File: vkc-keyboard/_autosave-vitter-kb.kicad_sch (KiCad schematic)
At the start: 70 parts, among them SW1 SW_SPST, SW10 SW_SPST, SW11 SW_SPST, SW12 SW_SPST, SW13 SW_SPST, SW14 SW_SPST, SW15 SW_SPST, SW16 SW_SPST, SW17 SW_SPST, SW18 SW_SPST, SW19 SW_SPST, SW2 SW_SPST, SW20 SW_SPST, SW21 SW_SPST, SW22 SW_SPST, SW23 SW_SPST, SW24 SW_SPST, SW25 SW_SPST, SW26 SW_SPST, SW27 SW_SPST, SW28 SW_SPST, SW29 SW_SPST, SW3 SW_SPST, SW30 SW_SPST, SW31 SW_SPST, SW32 SW_SPST, SW33 SW_SPST, SW34 SW_SPST, SW35 SW_SPST, SW4 SW_SPST, SW5 SW_SPST, SW6 SW_SPST, SW7 SW_SPST, SW8 SW_SPST, SW9 SW_SPST

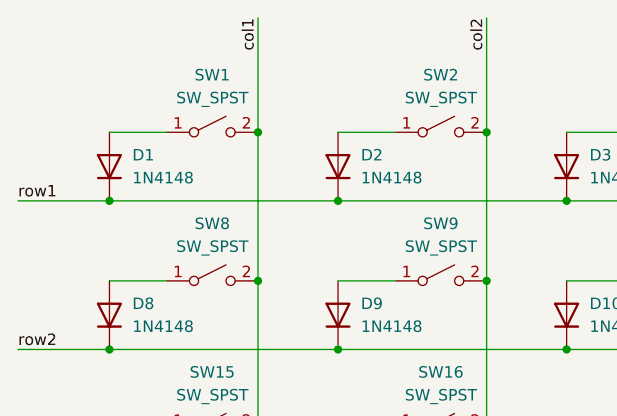
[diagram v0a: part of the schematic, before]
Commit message: use button outline footprint
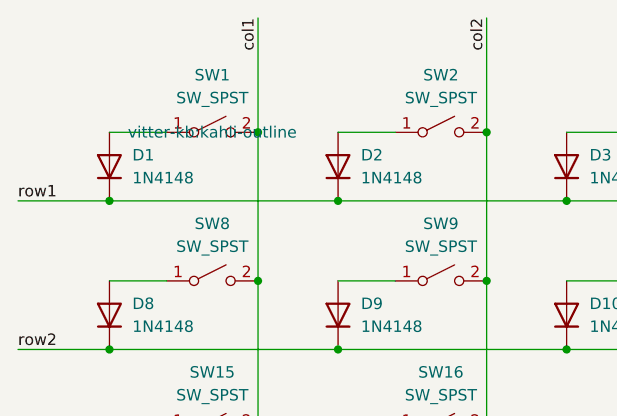
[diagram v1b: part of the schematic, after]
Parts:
- SW1, SW10, SW11, SW12, SW13, SW14, SW15, SW16, SW17, SW18, SW19, SW2, SW20, SW21, SW22, SW23, SW24, SW25, SW26, SW27, SW28, SW29, SW3, SW30, SW31, SW32, SW33, SW34, SW35, SW4, SW5, SW6, SW7, SW8, SW9: footprint vitter-kb:Kailh_socket_PG1350_reversible -> vitter-kb:kahli-outline
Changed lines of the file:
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@@
 			)
 		)
-		(property "Footprint" "vitter-kb:Kailh_socket_PG1350_reversible"
+		(property "Footprint" "vitter-kb:kahli-outline"
 			(at 196.85 38.1 0)
 			(effects
@@
 			)
 		)
-		(property "Footprint" "vitter-kb:Kailh_socket_PG1350_reversible"
+		(property "Footprint" "vitter-kb:kahli-outline"
 			(at 171.45 104.14 0)
 			(effects
@@
 			)
 		)
-		(property "Footprint" "vitter-kb:Kailh_socket_PG1350_reversible"
+		(property "Footprint" "vitter-kb:kahli-outline"
 			(at 95.25 54.61 0)
 			(effects
@@
 			)
 		)
-		(property "Footprint" "vitter-kb:Kailh_socket_PG1350_reversible"
+		(property "Footprint" "vitter-kb:kahli-outline"
 			(at 69.85 38.1 0)
 			(effects
@@
 			)
 		)
-		(property "Footprint" "vitter-kb:Kailh_socket_PG1350_reversible"
+		(property "Footprint" "vitter-kb:kahli-outline"
 			(at 95.25 71.12 0)
 			(effects
@@
 			)
 		)
-		(property "Footprint" "vitter-kb:Kailh_socket_PG1350_reversible"
+		(property "Footprint" "vitter-kb:kahli-outline"
 			(at 44.45 54.61 0)
 			(effects
@@
 			)
 		)
-		(property "Footprint" "vitter-kb:Kailh_socket_PG1350_reversible"
+		(property "Footprint" "vitter-kb:kahli-outline"
 			(at 69.85 87.63 0)
 			(effects
@@
 			)
 		)
-		(property "Footprint" "vitter-kb:Kailh_socket_PG1350_reversible"
+		(property "Footprint" "vitter-kb:kahli-outline"
 			(at 196.85 87.63 0)
 			(effects
@@
 			)
 		)
-		(property "Footprint" "vitter-kb:Kailh_socket_PG1350_reversible"
+		(property "Footprint" "vitter-kb:kahli-outline"
 			(at 171.45 38.1 0)
 			(effects
@@
 			)
 		)
-		(property "Footprint" "vitter-kb:Kailh_socket_PG1350_reversible"
+		(property "Footprint" "vitter-kb:kahli-outline"
 			(at 120.65 71.12 0)
 			(effects
@@
 			)
 		)
-		(property "Footprint" "vitter-kb:Kailh_socket_PG1350_reversible"
+		(property "Footprint" "vitter-kb:kahli-outline"
 			(at 120.65 104.14 0)
 			(effects
@@
 			)
 		)
-		(property "Footprint" "vitter-kb:Kailh_socket_PG1350_reversible"
+		(property "Footprint" "vitter-kb:kahli-outline"
 			(at 44.45 87.63 0)
 			(effects
@@
 			)
 		)
-		(property "Footprint" "vitter-kb:Kailh_socket_PG1350_reversible"
+		(property "Footprint" "vitter-kb:kahli-outline"
 			(at 146.05 104.14 0)
 			(effects
@@
 			)
 		)
-		(property "Footprint" "vitter-kb:Kailh_socket_PG1350_reversible"
+		(property "Footprint" "vitter-kb:kahli-outline"
 			(at 44.45 38.1 0)
 			(effects
@@
 					(size 1.27 1.27)
 				)
-				(hide yes)
 			)
 		)
@@
 			)
 		)
-		(property "Footprint" "vitter-kb:Kailh_socket_PG1350_reversible"
+		(property "Footprint" "vitter-kb:kahli-outline"
 			(at 196.85 54.61 0)
 			(effects
@@
 			)
 		)
-		(property "Footprint" "vitter-kb:Kailh_socket_PG1350_reversible"
+		(property "Footprint" "vitter-kb:kahli-outline"
 			(at 95.25 38.1 0)
 			(effects
@@
 			)
 		)
-		(property "Footprint" "vitter-kb:Kailh_socket_PG1350_reversible"
+		(property "Footprint" "vitter-kb:kahli-outline"
 			(at 44.45 71.12 0)
 			(effects
@@
 			)
 		)
-		(property "Footprint" "vitter-kb:Kailh_socket_PG1350_reversible"
+		(property "Footprint" "vitter-kb:kahli-outline"
 			(at 120.65 54.61 0)
 			(effects
@@
 			)
 		)
-		(property "Footprint" "vitter-kb:Kailh_socket_PG1350_reversible"
+		(property "Footprint" "vitter-kb:kahli-outline"
 			(at 69.85 71.12 0)
 			(effects
@@
 			)
 		)
-		(property "Footprint" "vitter-kb:Kailh_socket_PG1350_reversible"
+		(property "Footprint" "vitter-kb:kahli-outline"
 			(at 95.25 104.14 0)
 			(effects
@@
 			)
 		)
-		(property "Footprint" "vitter-kb:Kailh_socket_PG1350_reversible"
+		(property "Footprint" "vitter-kb:kahli-outline"
 			(at 120.65 87.63 0)
 			(effects
@@
 			)
 		)
-		(property "Footprint" "vitter-kb:Kailh_socket_PG1350_reversible"
+		(property "Footprint" "vitter-kb:kahli-outline"
 			(at 146.05 87.63 0)
 			(effects
@@
 			)
 		)
-		(property "Footprint" "vitter-kb:Kailh_socket_PG1350_reversible"
+		(property "Footprint" "vitter-kb:kahli-outline"
 			(at 44.45 104.14 0)
 			(effects
@@
 			)
 		)
-		(property "Footprint" "vitter-kb:Kailh_socket_PG1350_reversible"
+		(property "Footprint" "vitter-kb:kahli-outline"
 			(at 171.45 87.63 0)
 			(effects
@@
 			)
 		)
-		(property "Footprint" "vitter-kb:Kailh_socket_PG1350_reversible"
+		(property "Footprint" "vitter-kb:kahli-outline"
 			(at 69.85 104.14 0)
 			(effects
@@
 			)
 		)
-		(property "Footprint" "vitter-kb:Kailh_socket_PG1350_reversible"
+		(property "Footprint" "vitter-kb:kahli-outline"
 			(at 196.85 104.14 0)
 			(effects
@@
 			)
 		)
-		(property "Footprint" "vitter-kb:Kailh_socket_PG1350_reversible"
+		(property "Footprint" "vitter-kb:kahli-outline"
 			(at 146.05 38.1 0)
 			(effects
@@
 			)
 		)
-		(property "Footprint" "vitter-kb:Kailh_socket_PG1350_reversible"
+		(property "Footprint" "vitter-kb:kahli-outline"
 			(at 171.45 71.12 0)
 			(effects
@@
 			)
 		)
-		(property "Footprint" "vitter-kb:Kailh_socket_PG1350_reversible"
+		(property "Footprint" "vitter-kb:kahli-outline"
 			(at 69.85 54.61 0)
 			(effects
@@
 			)
 		)
-		(property "Footprint" "vitter-kb:Kailh_socket_PG1350_reversible"
+		(property "Footprint" "vitter-kb:kahli-outline"
 			(at 120.65 38.1 0)
 			(effects
@@
 			)
 		)
-		(property "Footprint" "vitter-kb:Kailh_socket_PG1350_reversible"
+		(property "Footprint" "vitter-kb:kahli-outline"
 			(at 146.05 71.12 0)
 			(effects
@@
 			)
 		)
-		(property "Footprint" "vitter-kb:Kailh_socket_PG1350_reversible"
+		(property "Footprint" "vitter-kb:kahli-outline"
 			(at 171.45 54.61 0)
 			(effects
@@
 			)
 		)
-		(property "Footprint" "vitter-kb:Kailh_socket_PG1350_reversible"
+		(property "Footprint" "vitter-kb:kahli-outline"
 			(at 146.05 54.61 0)
 			(effects
@@
 			)
 		)
-		(property "Footprint" "vitter-kb:Kailh_socket_PG1350_reversible"
+		(property "Footprint" "vitter-kb:kahli-outline"
 			(at 196.85 71.12 0)
 			(effects
@@
 			)
 		)
-		(property "Footprint" "vitter-kb:Kailh_socket_PG1350_reversible"
+		(property "Footprint" "vitter-kb:kahli-outline"
 			(at 95.25 87.63 0)
 			(effects
